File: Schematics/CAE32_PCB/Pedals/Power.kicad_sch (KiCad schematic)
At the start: 17 parts, among them U4 LDL1117

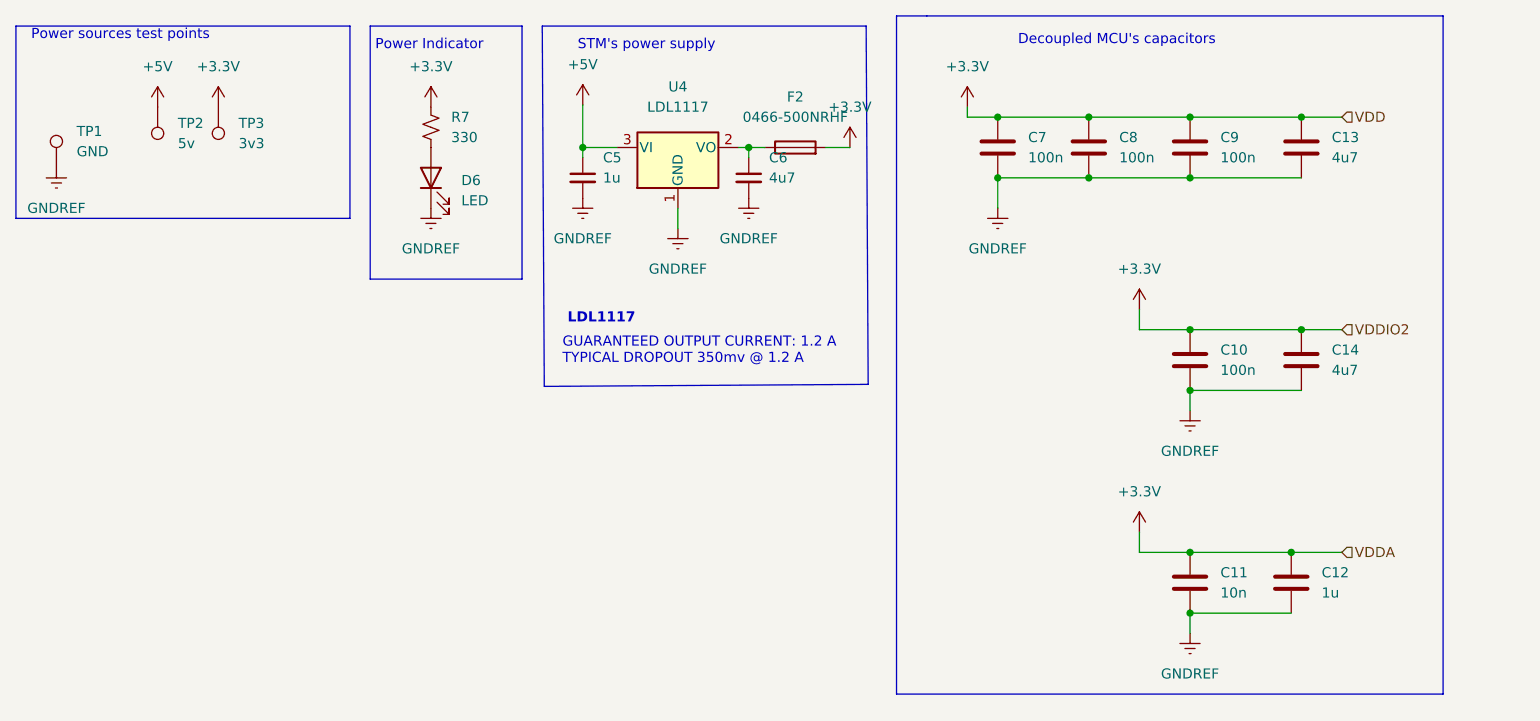
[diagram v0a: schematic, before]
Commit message: updated: Pcb design, fixed plane grounds and minor improvements, added stlink connector, updated BOM with the current market stock
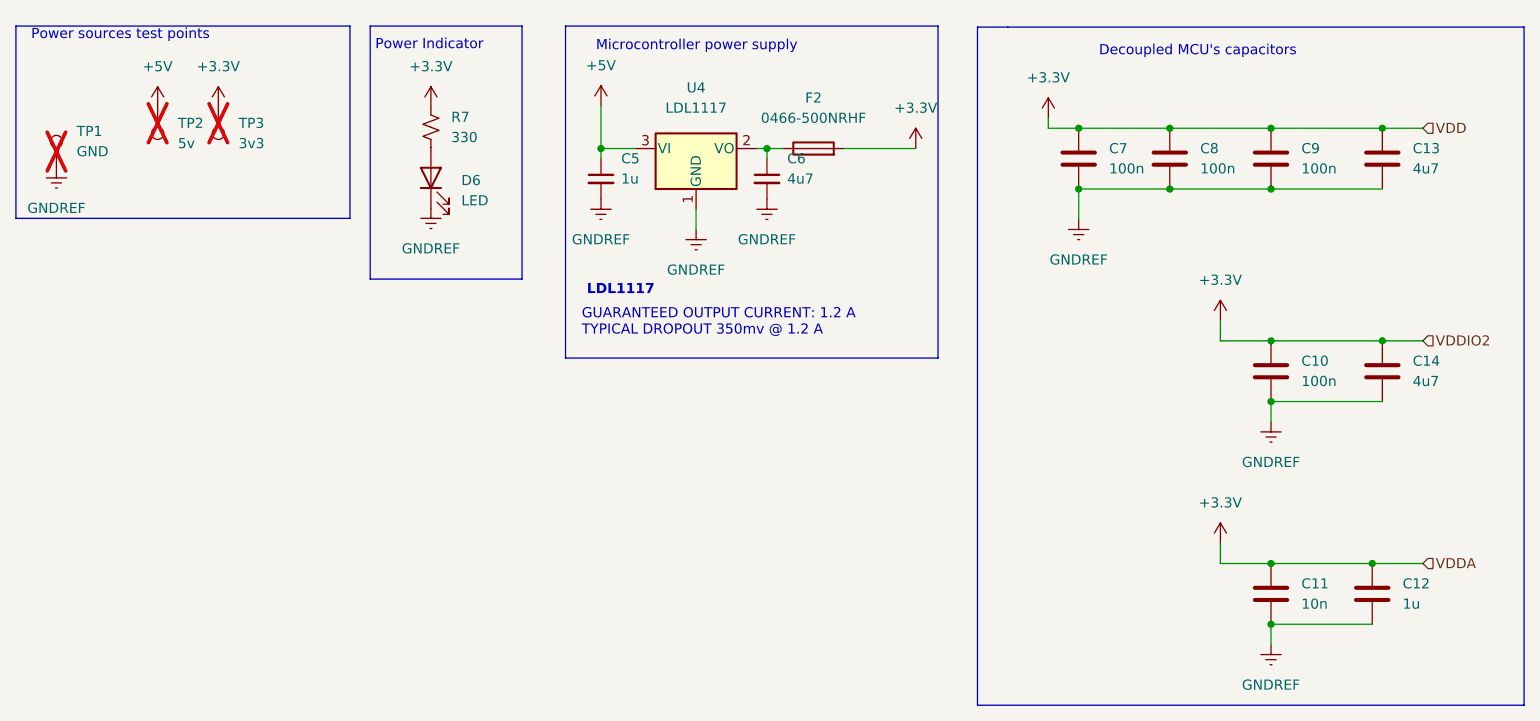
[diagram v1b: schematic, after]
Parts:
- C10, C7, C8, C9: Item c1591 -> C66501; LCSC_PART c1591 -> C66501; Vendor c1591 -> C66501
- R7: Item C25804 -> C21190; LCSC_PART C25804 -> C21190; Vendor C25804 -> C21190
- TP1, TP2, TP3: now not fitted
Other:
- note added: "Microcontroller power supply"
- note removed: "STM's power supply"
- moved on the sheet: C10, C11, C12, C13, C14, C5, C6, C7, C8, C9, F2, U4

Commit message: fixed: changed fuse footprint for the correct one(0805)
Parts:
- F2: footprint Fuse:Fuse_0603_1608Metric -> Fuse:Fuse_0805_2012Metric
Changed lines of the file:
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@@
 			)
 		)
-		(property "Footprint" "Fuse:Fuse_0603_1608Metric"
+		(property "Footprint" "Fuse:Fuse_0805_2012Metric"
 			(at 119.126 38.735 90)
 			(effects

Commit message: fixed: changed fuse footprint to 1206
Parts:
- F2: footprint Fuse:Fuse_0805_2012Metric -> Fuse:Fuse_1206_3216Metric
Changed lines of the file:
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@@
 			)
 		)
-		(property "Footprint" "Fuse:Fuse_0805_2012Metric"
+		(property "Footprint" "Fuse:Fuse_1206_3216Metric"
 			(at 119.126 38.735 90)
 			(effects
